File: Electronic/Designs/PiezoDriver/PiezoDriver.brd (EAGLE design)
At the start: 50 x 50 mm, 35 parts

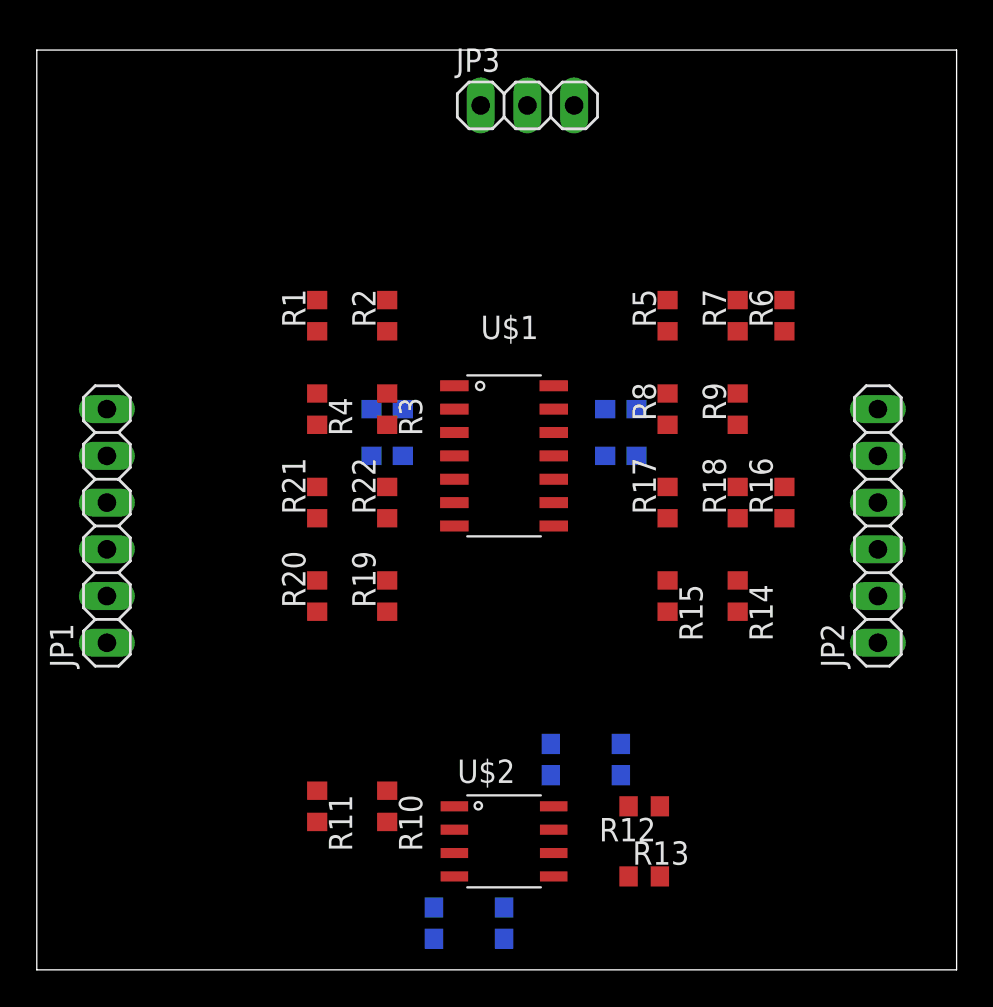
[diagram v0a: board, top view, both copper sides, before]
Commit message: Added to Piezo Driver Board
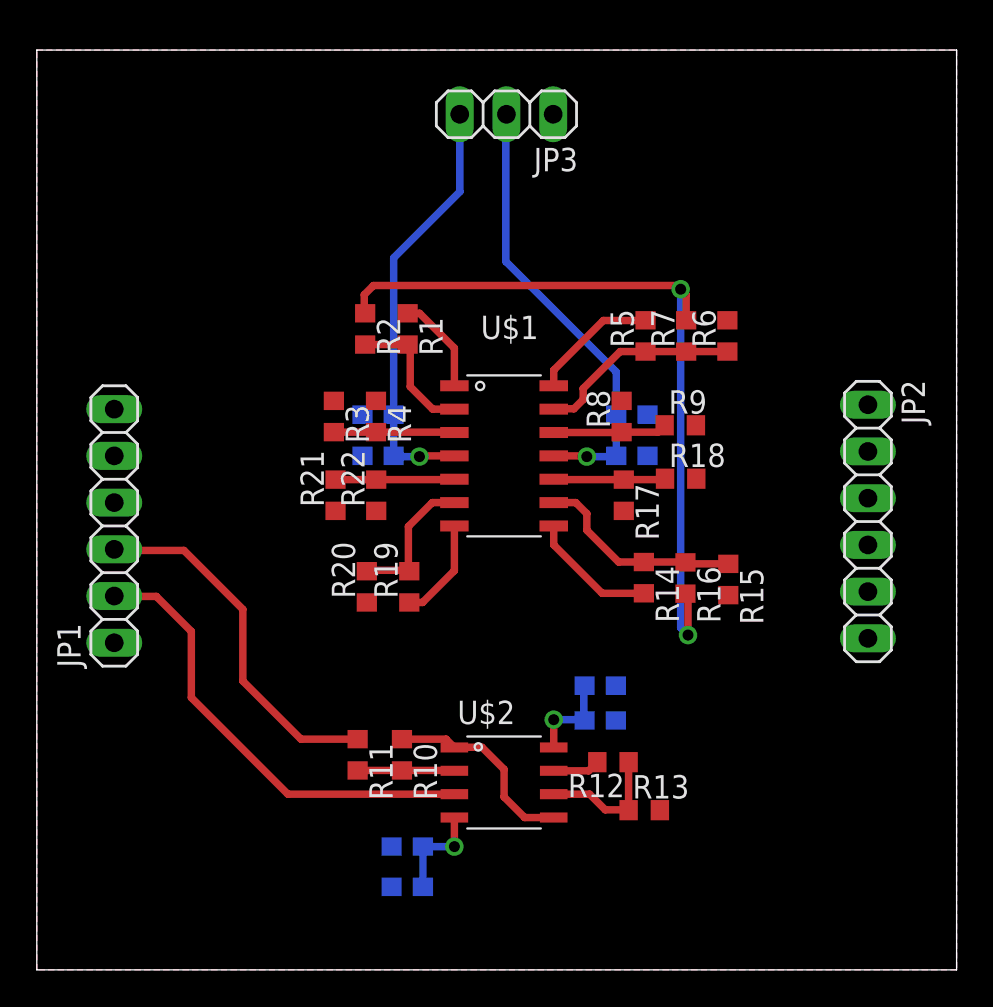
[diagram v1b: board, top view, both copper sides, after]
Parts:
- R20: value 40k -> 10k
- moved R16 6.76 mm to (35.3, 21.3), turned to 270 degrees
- moved C8 6.71 mm to (20.1, 6.70), turned to 0 degrees
- moved R14 5.20 mm to (33.0, 21.3)
- moved R1 4.97 mm to (20.2, 34.8), turned to 270 degrees
- moved C7 4.17 mm to (30.6, 15.4), turned to 180 degrees
- moved R13 3.60 mm to (33.0, 8.68)
- moved R11 3.56 mm to (17.4, 11.7)
- moved C5 3.43 mm to (30.6, 13.6), turned to 180 degrees
- moved R15 3.42 mm to (37.6, 21.2)
- moved R18 3.36 mm to (35.0, 26.7), turned to 0 degrees
- moved R6 3.29 mm to (37.5, 34.5)
- moved R9 3.24 mm to (35.0, 29.6), turned to 0 degrees
- moved R4 3.22 mm to (18.4, 30.1)
- moved U$2 3.20 mm to (25.4, 10.8)
- moved R7 3.01 mm to (35.3, 34.5)
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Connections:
- net B: now also JP1.2; no longer JP1.3
- net VREF: now also JP1.3; no longer JP1.2
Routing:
- net Z: track 0.00 -> 41.6 mm, vias 0 -> 2
- net V-: track 0.00 -> 30.0 mm, vias 0 -> 2
- net V+: track 0.00 -> 28.5 mm, vias 0 -> 2
- net B: track 0.00 -> 25.1 mm
- net VREF: track 0.00 -> 19.8 mm
- net N$4: track 0.00 -> 11.4 mm
- net N$5: track 0.00 -> 11.1 mm
- net N$7: track 0.00 -> 10.9 mm
- net N$2: track 0.00 -> 7.77 mm
- net N$1: track 0.00 -> 7.56 mm
- net N$10: track 0.00 -> 7.03 mm
- net YNEG: track 0.00 -> 7.02 mm
- net XNEG: track 0.00 -> 6.96 mm
- net N$3: track 0.00 -> 6.56 mm
- net N$13: track 0.00 -> 6.47 mm
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- added copper zone on layer 1, net GND
- added copper zone on layer 16, net GND

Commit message: Added to piezo board
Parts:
- moved C5 2.80 mm to (30.6, 10.8)
- moved U$2 2.80 mm to (25.4, 8.02)
- moved C8 2.80 mm to (20.1, 3.90)
- moved R13 2.80 mm to (33.0, 5.88)
- moved R10 2.80 mm to (19.9, 8.89)
- moved R11 2.80 mm to (17.4, 8.89)
- moved R12 2.80 mm to (31.3, 8.49)
- moved C7 2.60 mm to (30.6, 12.8)
- moved C6 1.80 mm to (20.1, 6.31)
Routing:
- net VREF: track 19.8 -> 66.8 mm, vias 0 -> 3
- net X: track 0.00 -> 44.9 mm, vias 0 -> 2
- net XPOS: track 5.37 -> 43.8 mm, vias 0 -> 2
- net Z: track 41.6 -> 76.4 mm, vias 2 -> 4
- net XNEG: track 6.96 -> 36.4 mm, vias 0 -> 4
- net BIAS: track 2.56 -> 26.2 mm
- net YNEG: track 7.02 -> 28.2 mm, vias 0 -> 2
- net B: track 25.1 -> 27.9 mm

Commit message: added to piezo board
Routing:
- net Y: track 0.00 -> 58.9 mm, vias 0 -> 4
- net YPOS: track 5.60 -> 43.0 mm, vias 0 -> 2
- net YNEG: vias 2 -> 0
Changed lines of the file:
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@@
 <wire x1="37.6" y1="26.7" x2="35.85" y2="26.7" width="0.4064" layer="1"/>
 <wire x1="35.85" y1="26.7" x2="37.5" y2="26.7" width="0.4064" layer="1"/>
-<wire x1="37.1" y1="26.2" x2="37.1" y2="12.2" width="0.4064" layer="16"/>
-<wire x1="37.1" y1="12.2" x2="36.8" y2="11.9" width="0.4064" layer="16"/>
-<via x="36.8" y="11.9" extent="1-16" drill="0.6"/>
-<wire x1="36.8" y1="11.9" x2="18.3" y2="11.9" width="0.4064" layer="1"/>
+<wire x1="37.1" y1="26.2" x2="37.1" y2="12.3" width="0.4064" layer="16"/>
+<wire x1="37.1" y1="12.3" x2="36.4" y2="11.9" width="0.4064" layer="16"/>
+<via x="36.4" y="11.9" extent="1-16" drill="0.6"/>
+<wire x1="36.4" y1="11.9" x2="18.3" y2="11.9" width="0.4064" layer="1"/>
 <wire x1="18.3" y1="11.9" x2="17.4" y2="11" width="0.4064" layer="1"/>
 <wire x1="17.4" y1="11" x2="17.4" y2="9.78" width="0.4064" layer="1"/>
@@
 <wire x1="30" y1="8.02" x2="30.47" y2="8.49" width="0.4064" layer="1"/>
 <wire x1="45.18" y1="20.56" x2="43.96" y2="20.56" width="0.4064" layer="1"/>
-<wire x1="43.96" y1="20.56" x2="42.1" y2="18.7" width="0.4064" layer="1"/>
-<wire x1="42.1" y1="18.7" x2="42.1" y2="12.9" width="0.4064" layer="1"/>
-<wire x1="42.1" y1="12.9" x2="39.9" y2="10.7" width="0.4064" layer="1"/>
+<wire x1="43.96" y1="20.56" x2="42.6" y2="19.2" width="0.4064" layer="1"/>
+<wire x1="42.6" y1="19.2" x2="42.6" y2="13.3" width="0.4064" layer="1"/>
+<wire x1="42.6" y1="13.3" x2="39.9" y2="10.7" width="0.4064" layer="1"/>
 <wire x1="39.9" y1="10.7" x2="31.7" y2="10.7" width="0.4064" layer="1"/>
 <wire x1="31.7" y1="10.7" x2="30.5" y2="9.5" width="0.4064" layer="1"/>
@@
 <contactref element="R15" pad="2"/>
 <contactref element="R21" pad="1"/>
-<wire x1="16.24" y1="24.95" x2="37.59" y2="20.37" width="0" layer="19" extent="1-1"/>
-<wire x1="4.21" y1="27.94" x2="16.24" y2="24.95" width="0" layer="19" extent="1-1"/>
+<wire x1="4.21" y1="27.94" x2="11.76" y2="27.94" width="0.4064" layer="1"/>
+<wire x1="11.76" y1="27.94" x2="12.9" y2="26.8" width="0.4064" layer="1"/>
+<via x="12.9" y="26.8" extent="1-16" drill="0.6"/>
+<wire x1="12.9" y1="26.8" x2="12.9" y2="15.4" width="0.4064" layer="16"/>
+<wire x1="12.9" y1="15.4" x2="14.7" y2="13.5" width="0.4064" layer="16"/>
+<via x="14.7" y="13.5" extent="1-16" drill="0.6"/>
+<wire x1="14.7" y1="13.5" x2="38.8" y2="13.5" width="0.4064" layer="1"/>
+<via x="38.8" y="13.5" extent="1-16" drill="0.6"/>
+<wire x1="38.8" y1="13.5" x2="38.8" y2="18.2" width="0.4064" layer="16"/>
+<wire x1="38.8" y1="18.3" x2="38.8" y2="18.2" width="0.4064" layer="16"/>
+<via x="38.8" y="18.2" extent="1-16" drill="0.6"/>
+<wire x1="38.8" y1="18.2" x2="38.8" y2="19.16" width="0.4064" layer="1"/>
+<wire x1="38.8" y1="19.16" x2="37.59" y2="20.37" width="0.4064" layer="1"/>
+<wire x1="16.24" y1="24.95" x2="14.75" y2="24.95" width="0.4064" layer="1"/>
+<wire x1="14.75" y1="24.95" x2="12.9" y2="26.8" width="0.4064" layer="1"/>
 </signal>
 <signal name="YNEG">
@@
 <wire x1="30.73" y1="20.47" x2="28.1" y2="23.1" width="0.4064" layer="1"/>
 <wire x1="28.1" y1="23.1" x2="28.1" y2="24.13" width="0.4064" layer="1"/>
-<wire x1="45.18" y1="23.1" x2="41.6" y2="23.1" width="0.4064" layer="1"/>
-<wire x1="41.6" y1="23.1" x2="40.7" y2="22.2" width="0.4064" layer="1"/>
-<via x="40.7" y="22.2" extent="1-16" drill="0.6"/>
-<wire x1="40.7" y1="22.2" x2="40.7" y2="16.9" width="0.4064" layer="16"/>
-<wire x1="40.7" y1="16.9" x2="40.5" y2="16.5" width="0.4064" layer="16"/>
+<wire x1="45.18" y1="23.1" x2="42" y2="23.1" width="0.4064" layer="1"/>
+<wire x1="42" y1="23.1" x2="41.1" y2="22.2" width="0.4064" layer="1"/>
 <wire x1="33" y1="20.47" x2="33" y2="18" width="0.4064" layer="1"/>
 <wire x1="33" y1="18" x2="34.5" y2="16.5" width="0.4064" layer="1"/>
-<wire x1="34.5" y1="16.5" x2="40.5" y2="16.5" width="0.4064" layer="1"/>
-<via x="40.5" y="16.5" extent="1-16" drill="0.6"/>
+<wire x1="34.5" y1="16.5" x2="40.9" y2="16.5" width="0.4064" layer="1"/>
+<wire x1="41.1" y1="22.2" x2="41.1" y2="16.7" width="0.4064" layer="1"/>
+<wire x1="41.1" y1="16.7" x2="40.9" y2="16.5" width="0.4064" layer="1"/>
 </signal>
 <signal name="N$4">
@@
 <wire x1="20.97" y1="19.97" x2="22.7" y2="21.7" width="0.4064" layer="1"/>
 <wire x1="22.7" y1="21.7" x2="22.7" y2="24.13" width="0.4064" layer="1"/>
-<wire x1="22.7" y1="24.13" x2="45.18" y2="25.64" width="0" layer="19" extent="1-1"/>
+<wire x1="45.18" y1="25.64" x2="41.44" y2="25.64" width="0.4064" layer="1"/>
+<wire x1="41.44" y1="25.64" x2="40.8" y2="25" width="0.4064" layer="1"/>
+<via x="40.8" y="25" extent="1-16" drill="0.6" shape="square"/>
+<wire x1="40.8" y1="25" x2="40.8" y2="15" width="0.4064" layer="16"/>
+<wire x1="40.8" y1="15" x2="40.6" y2="14.8" width="0.4064" layer="16"/>
+<via x="40.6" y="14.8" extent="1-16" drill="0.6"/>
+<wire x1="40.6" y1="14.8" x2="25.42" y2="14.8" width="0.4064" layer="1"/>
+<wire x1="25.42" y1="14.8" x2="20.25" y2="19.97" width="0.4064" layer="1"/>
 </signal>
 <signal name="N$13">

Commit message: Added to piezo driver
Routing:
- net V-: track 30.2 -> 56.3 mm, vias 2 -> 4
- net V+: track 28.7 -> 47.9 mm
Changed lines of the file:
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@@
 <wire x1="25.5" y1="38.5" x2="25.5" y2="46.48" width="0.4064" layer="16"/>
 <wire x1="25.5" y1="46.48" x2="25.53" y2="46.51" width="0.4064" layer="16"/>
-<wire x1="20.99" y1="6.31" x2="28.1" y2="27.94" width="0" layer="19" extent="1-16"/>
+<wire x1="20.99" y1="6.31" x2="20.99" y2="14.89" width="0.4064" layer="16"/>
+<wire x1="20.99" y1="14.89" x2="24.2" y2="18.2" width="0.4064" layer="16"/>
+<via x="24.2" y="18.2" extent="1-16" drill="0.6"/>
+<via x="26.7" y="20.6" extent="1-16" drill="0.6"/>
+<wire x1="26.7" y1="20.6" x2="26.8" y2="20.6" width="0.4064" layer="16"/>
+<wire x1="26.8" y1="20.6" x2="31.5" y2="25.3" width="0.4064" layer="16"/>
+<wire x1="31.5" y1="25.3" x2="31.5" y2="27.94" width="0.4064" layer="16"/>
+<wire x1="24.2" y1="18.2" x2="24.3" y2="18.2" width="0.4064" layer="1"/>
+<wire x1="24.3" y1="18.2" x2="26.7" y2="20.6" width="0.4064" layer="1"/>
 </signal>
 <signal name="V+">
@@
 <wire x1="23" y1="43.8" x2="23" y2="46.5" width="0.4064" layer="16"/>
 <wire x1="23" y1="46.5" x2="22.99" y2="46.51" width="0.4064" layer="16"/>
-<wire x1="29.78" y1="12.85" x2="22.7" y2="27.94" width="0" layer="19" extent="1-16"/>
+<wire x1="29.78" y1="12.85" x2="29.68" y2="15.12" width="0.4064" layer="16"/>
+<wire x1="29.68" y1="15.12" x2="19.5" y2="25.4" width="0.4064" layer="16"/>
+<wire x1="19.5" y1="25.4" x2="19.4" y2="27.94" width="0.4064" layer="16"/>
 </signal>
 <signal name="N$1">
@@
 <wire x1="45.18" y1="25.64" x2="41.44" y2="25.64" width="0.4064" layer="1"/>
 <wire x1="41.44" y1="25.64" x2="40.8" y2="25" width="0.4064" layer="1"/>
-<via x="40.8" y="25" extent="1-16" drill="0.6" shape="square"/>
+<via x="40.8" y="25" extent="1-16" drill="0.6"/>
 <wire x1="40.8" y1="25" x2="40.8" y2="15" width="0.4064" layer="16"/>
 <wire x1="40.8" y1="15" x2="40.6" y2="14.8" width="0.4064" layer="16"/>
 <via x="40.6" y="14.8" extent="1-16" drill="0.6"/>
-<wire x1="40.6" y1="14.8" x2="25.42" y2="14.8" width="0.4064" layer="1"/>
-<wire x1="25.42" y1="14.8" x2="20.25" y2="19.97" width="0.4064" layer="1"/>
+<wire x1="40.6" y1="14.8" x2="25.02" y2="14.8" width="0.4064" layer="1"/>
+<wire x1="25.02" y1="14.8" x2="20.25" y2="19.97" width="0.4064" layer="1"/>
 </signal>
 <signal name="N$13">

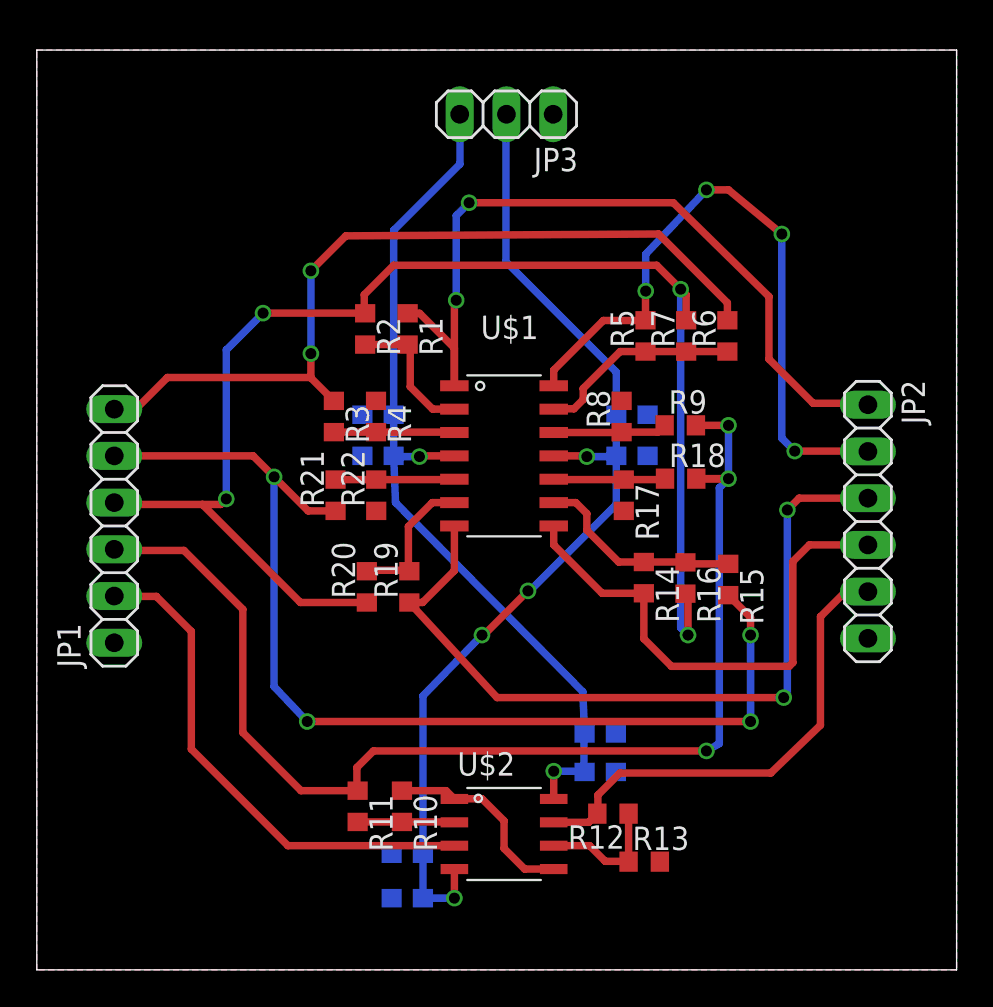
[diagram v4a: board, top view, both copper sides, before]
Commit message: Added better Cmake QT Find and added dac2 piezo and tun boards
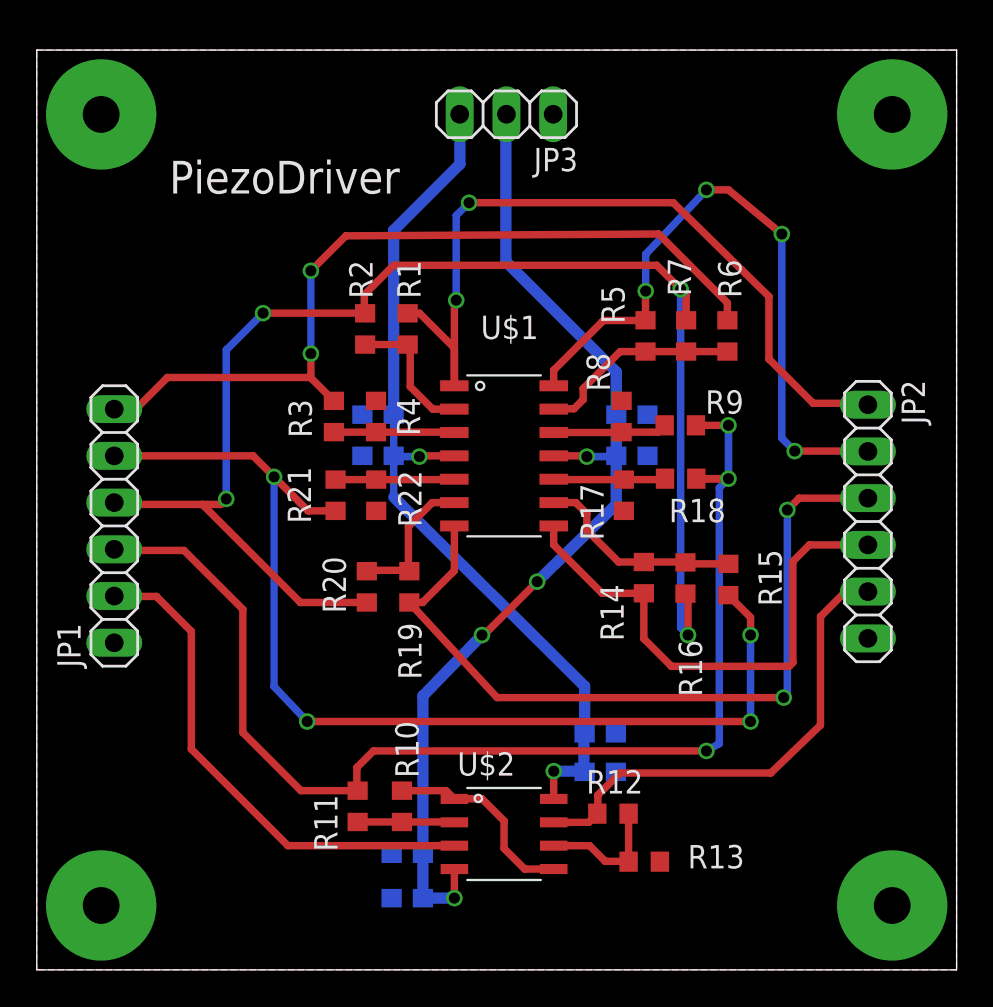
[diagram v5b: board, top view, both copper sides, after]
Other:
- board text added: "PiezoDriver"
